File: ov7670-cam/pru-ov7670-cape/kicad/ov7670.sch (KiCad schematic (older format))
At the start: 22 parts, among them P1 OV7670_1, P5 OV7670_2

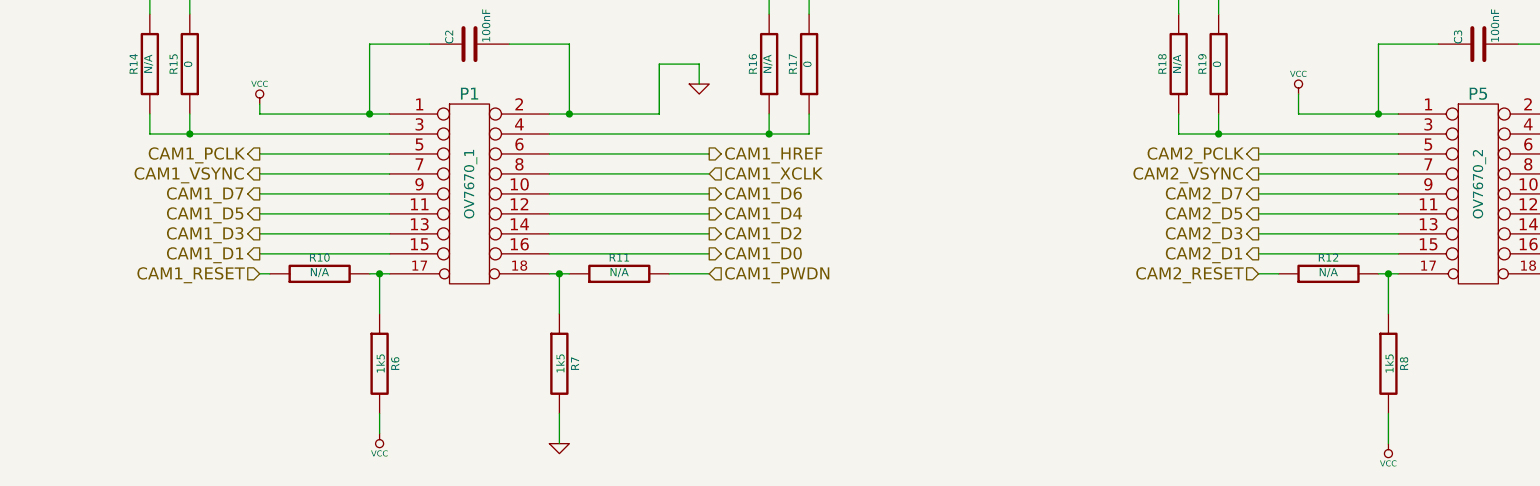
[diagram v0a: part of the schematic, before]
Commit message: pru-ov7670-cape: Fix erroneous PCLK/VSYNC pin connection
The two OV7670 pins were inadvertently swapped.

Signed-off-by: Dimitar Dimitrov <dinuxbg@gmail.com>
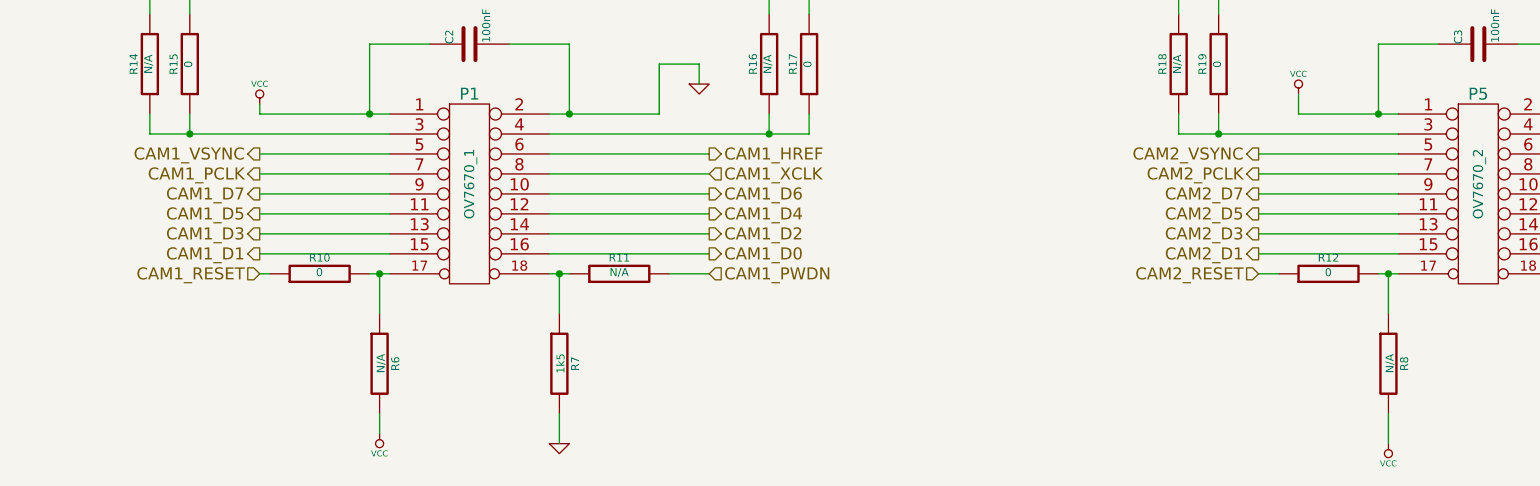
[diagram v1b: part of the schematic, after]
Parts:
- R10, R12: value N/A -> 0
- R6, R8: value 1k5 -> N/A
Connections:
- net CAM1_PCLK: now also P1.7; no longer P1.5
- net CAM1_VSYNC: now also P1.5; no longer P1.7
- net CAM2_PCLK: now also P5.7; no longer P5.5
- net CAM2_VSYNC: now also P5.5; no longer P5.7
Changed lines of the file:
@@
 Sheet 5 5
 Title ""
-Date "17 mar 2015"
+Date "29 mar 2015"
 Rev ""
 Comp ""
@@
 Text HLabel 10300 3150 2    60   Input ~ 0
 CAM1_SIO_C
-Text HLabel 2400 4500 0    60   Output ~ 0
+Text HLabel 2400 4400 0    60   Output ~ 0
 CAM1_VSYNC
 Text HLabel 2400 4600 0    60   Output ~ 0
@@
 Text HLabel 2400 5000 0    60   Input ~ 0
 CAM1_RESET
-Text HLabel 2400 4400 0    60   Output ~ 0
+Text HLabel 2400 4500 0    60   Output ~ 0
 CAM1_PCLK
 Text HLabel 10300 3250 2    60   BiDi ~ 0
@@
 Text HLabel 7400 4600 0    60   Output ~ 0
 CAM2_D7
+Text HLabel 7400 4400 0    60   Output ~ 0
+CAM2_VSYNC
 Text HLabel 7400 4500 0    60   Output ~ 0
-CAM2_VSYNC
-Text HLabel 7400 4400 0    60   Output ~ 0
 CAM2_PCLK
 Text HLabel 10300 3350 2    60   Input ~ 0
@@
 P 3000 5450
 F 0 "R6" V 3080 5450 40  0000 C CNN
-F 1 "1k5" V 3007 5451 40  0000 C CNN
+F 1 "N/A" V 3007 5451 40  0000 C CNN
 F 2 "~" V 2930 5450 30  0000 C CNN
 F 3 "~" H 3000 5450 30  0000 C CNN
@@
 P 8050 5450
 F 0 "R8" V 8130 5450 40  0000 C CNN
-F 1 "1k5" V 8057 5451 40  0000 C CNN
+F 1 "N/A" V 8057 5451 40  0000 C CNN
 F 2 "~" V 7980 5450 30  0000 C CNN
 F 3 "~" H 8050 5450 30  0000 C CNN
@@
 P 2700 5000
 F 0 "R10" V 2780 5000 40  0000 C CNN
-F 1 "N/A" V 2707 5001 40  0000 C CNN
+F 1 "0" V 2707 5001 40  0000 C CNN
 F 2 "~" V 2630 5000 30  0000 C CNN
 F 3 "~" H 2700 5000 30  0000 C CNN
@@
 P 7750 5000
 F 0 "R12" V 7830 5000 40  0000 C CNN
-F 1 "N/A" V 7757 5001 40  0000 C CNN
+F 1 "0" V 7757 5001 40  0000 C CNN
 F 2 "~" V 7680 5000 30  0000 C CNN
 F 3 "~" H 7750 5000 30  0000 C CNN
@@
 $EndComp
 Wire Wire Line
-	2400 4400 3050 4400
-Wire Wire Line
-	2400 4500 3050 4500
-Wire Wire Line
 	2400 4600 3050 4600
 Wire Wire Line
@@
 Wire Wire Line
 	7600 4200 7600 4100
-Wire Wire Line
-	7400 4400 8100 4400
-Wire Wire Line
-	7400 4500 8100 4500
 Wire Wire Line
 	7400 4600 8100 4600
@@
 Text Notes 1600 2550 0    60   ~ 0
 Note: I2C2 pull-ups are already present on sheet P9
+Wire Wire Line
+	8100 4400 7400 4400
+Wire Wire Line
+	7400 4500 8100 4500
+Wire Wire Line
+	3050 4400 2400 4400
+Wire Wire Line
+	2400 4500 3050 4500
 $EndSCHEMATC
